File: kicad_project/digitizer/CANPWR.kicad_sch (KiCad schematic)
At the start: 14 parts, among them IC201 MAX3059ASA+T UPSTREAM, IC202 MAX6035AAUR50+T, IC203 MAX3059ASA+T DOWNSTREAM, IC204 MAX6043BAUT33+T, J201 DT15-4P (UPSTREAM), J202 DT06-4S (DOWNSTREAM)

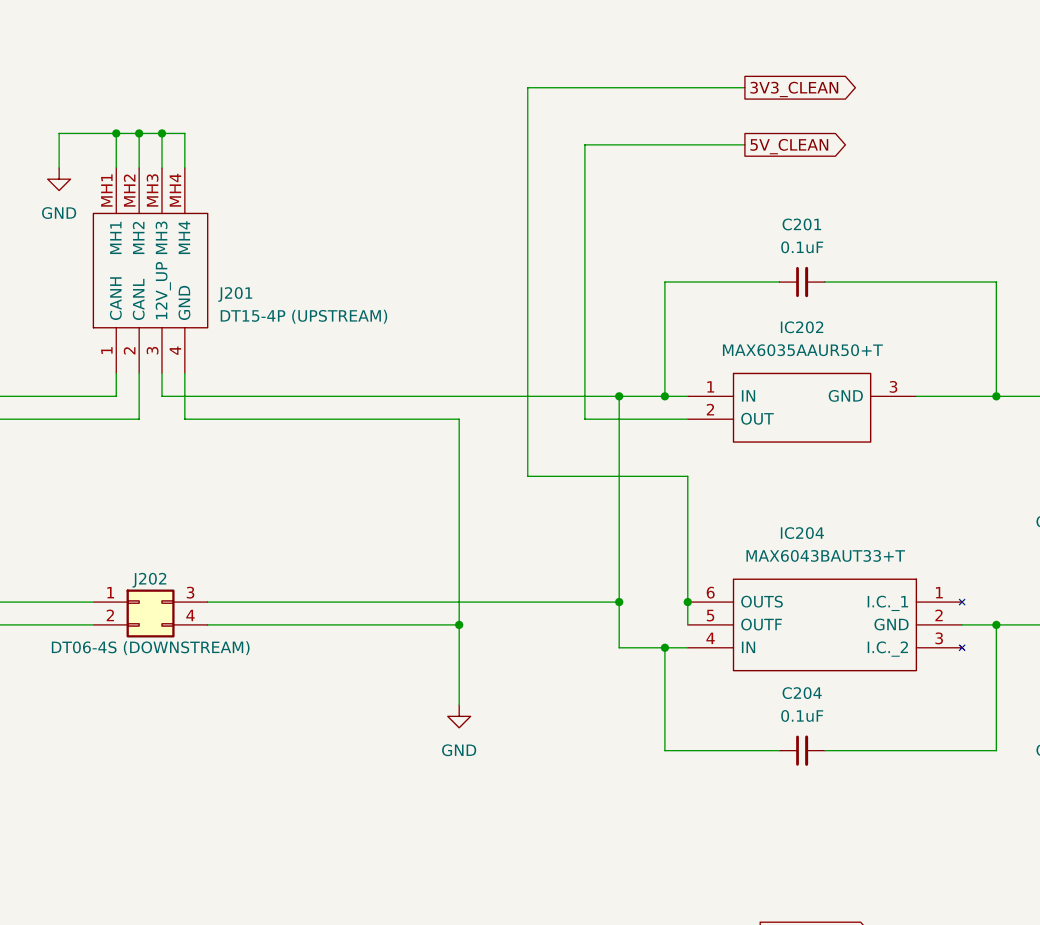
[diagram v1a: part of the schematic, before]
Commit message: added 12V_CLEAN label to schematic; added planes for 12V_CLEAN and 3V3_CLEAN to layout
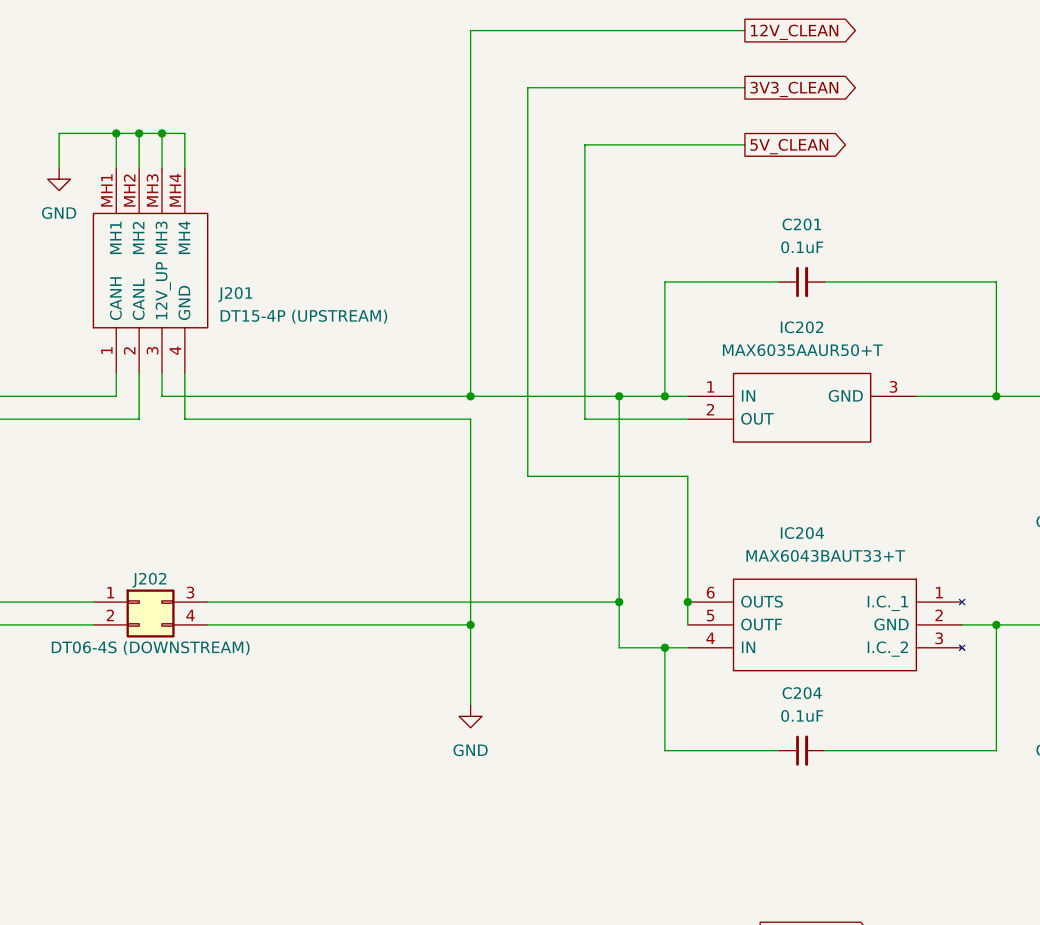
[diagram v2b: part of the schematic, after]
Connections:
- net 12V_CLEAN: now reaches C201.1, C204.1, IC202.1 (IN), IC204.4 (IN), J201.3 (12V_UP), J202.3 (12V_DOWN)
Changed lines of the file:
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@@
   (junction (at 203.2 83.82) (diameter 0) (color 0 0 0 0)
   )
+  (junction (at 186.69 86.36) (diameter 0) (color 0 0 0 0)
+  )
   (junction (at 210.82 83.82) (diameter 0) (color 0 0 0 0)
   )
-  (junction (at 185.42 86.36) (diameter 0) (color 0 0 0 0)
-  )
   (junction (at 208.28 88.9) (diameter 0) (color 0 0 0 0)
   )
@@
   (junction (at 64.77 83.82) (diameter 0) (color 0 0 0 0)
   )
+  (junction (at 186.69 60.96) (diameter 0) (color 0 0 0 0)
+  )
   (junction (at 55.88 86.36) (diameter 0) (color 0 0 0 0)
   )
@@
     (stroke (width 0) (type default) (color 0 0 0 0))
   )
-  (wire (pts (xy 185.42 86.36) (xy 185.42 95.25))
+  (wire (pts (xy 186.69 86.36) (xy 186.69 95.25))
     (stroke (width 0) (type default) (color 0 0 0 0))
   )
@@
     (stroke (width 0) (type default) (color 0 0 0 0))
   )
+  (wire (pts (xy 217.17 20.32) (xy 186.69 20.32))
+    (stroke (width 0) (type default) (color 0 0 0 0))
+  )
   (wire (pts (xy 236.22 129.54) (xy 236.22 133.35))
     (stroke (width 0) (type default) (color 0 0 0 0))
@@
     (stroke (width 0) (type default) (color 0 0 0 0))
   )
-  (wire (pts (xy 154.94 63.5) (xy 185.42 63.5))
+  (wire (pts (xy 154.94 63.5) (xy 186.69 63.5))
     (stroke (width 0) (type default) (color 0 0 0 0))
   )
@@
     (stroke (width 0) (type default) (color 0 0 0 0))
   )
-  (wire (pts (xy 152.4 60.96) (xy 203.2 60.96))
+  (wire (pts (xy 152.4 60.96) (xy 186.69 60.96))
     (stroke (width 0) (type default) (color 0 0 0 0))
   )
@@
     (stroke (width 0) (type default) (color 0 0 0 0))
   )
-  (wire (pts (xy 185.42 63.5) (xy 185.42 86.36))
+  (wire (pts (xy 186.69 63.5) (xy 186.69 86.36))
     (stroke (width 0) (type default) (color 0 0 0 0))
   )
@@
     (stroke (width 0) (type default) (color 0 0 0 0))
   )
+  (wire (pts (xy 186.69 20.32) (xy 186.69 60.96))
+    (stroke (width 0) (type default) (color 0 0 0 0))
+  )
   (wire (pts (xy 251.46 86.36) (xy 251.46 95.25))
     (stroke (width 0) (type default) (color 0 0 0 0))
@@
     (stroke (width 0) (type default) (color 0 0 0 0))
   )
-  (wire (pts (xy 157.48 86.36) (xy 185.42 86.36))
+  (wire (pts (xy 157.48 86.36) (xy 186.69 86.36))
     (stroke (width 0) (type default) (color 0 0 0 0))
   )
@@
   )
   (wire (pts (xy 210.82 63.5) (xy 199.39 63.5))
+    (stroke (width 0) (type default) (color 0 0 0 0))
+  )
+  (wire (pts (xy 186.69 60.96) (xy 203.2 60.96))
     (stroke (width 0) (type default) (color 0 0 0 0))
   )
@@
     (effects (font (size 1.27 1.27)) (justify left))
     (property "Intersheet References" "${INTERSHEET_REFS}" (id 0) (at 228.715 32.9406 0)
+      (effects (font (size 1.27 1.27)) (justify left) hide)
+    )
+  )
+  (global_label "12V_CLEAN" (shape output) (at 217.17 20.32 0) (fields_autoplaced)
+    (effects (font (size 1.27 1.27)) (justify left))
+    (property "Intersheet References" "${INTERSHEET_REFS}" (id 0) (at 229.9245 20.2406 0)
       (effects (font (size 1.27 1.27)) (justify left) hide)
     )
@@
     (pin "6")
   )
-  (symbol (lib_id "power:GND") (at 185.42 95.25 0) (unit 1)
+  (symbol (lib_id "power:GND") (at 186.69 95.25 0) (unit 1)
     (in_bom yes) (on_board yes) (fields_autoplaced)
-    (property "Reference" "#PWR0205" (id 0) (at 185.42 101.6 0)
-      (effects (font (size 1.27 1.27)) hide)
-    )
-    (property "Value" "GND" (id 1) (at 185.42 100.33 0))
-    (property "Footprint" "" (id 2) (at 185.42 95.25 0)
-      (effects (font (size 1.27 1.27)) hide)
-    )
-    (property "Datasheet" "" (id 3) (at 185.42 95.25 0)
-      (effects (font (size 1.27 1.27)) hide)
-    )
+    (property "Reference" "#PWR0205" (id 0) (at 186.69 101.6 0)
+      (effects (font (size 1.27 1.27)) hide)
+    )
+    (property "Value" "GND" (id 1) (at 186.69 100.33 0))
+    (property "Footprint" "" (id 2) (at 186.69 95.25 0)
+      (effects (font (size 1.27 1.27)) hide)
+    )
+    (property "Datasheet" "" (id 3) (at 186.69 95.25 0)
+      (effects (font (size 1.27 1.27)) hide)
+    )

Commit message: updated schematic to use all 0805 parts (both caps and resistors)
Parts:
- C201, C202, C203, C204: footprint Capacitor_SMD:C_2220_5650Metric_Pad1.97x5.40mm_HandSolder -> Capacitor_SMD:C_0805_2012Metric_Pad1.18x1.45mm_HandSolder
- R201, R202, R203: footprint Resistor_SMD:R_2512_6332Metric_Pad1.40x3.35mm_HandSolder -> Resistor_SMD:R_0805_2012Metric_Pad1.20x1.40mm_HandSolder
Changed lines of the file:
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@@
       (effects (font (size 1.27 1.27)) (justify left))
     )
-    (property "Footprint" "Resistor_SMD:R_2512_6332Metric_Pad1.40x3.35mm_HandSolder" (id 2) (at 236.22 127 0)
+    (property "Footprint" "Resistor_SMD:R_0805_2012Metric_Pad1.20x1.40mm_HandSolder" (id 2) (at 236.22 127 0)
       (effects (font (size 1.27 1.27)) hide)
     )
@@
     (property "Reference" "C202" (id 0) (at 62.23 54.61 90))
     (property "Value" "0.1uF" (id 1) (at 62.23 57.15 90))
-    (property "Footprint" "Capacitor_SMD:C_2220_5650Metric_Pad1.97x5.40mm_HandSolder" (id 2) (at 62.23 60.96 0)
+    (property "Footprint" "Capacitor_SMD:C_0805_2012Metric_Pad1.18x1.45mm_HandSolder" (id 2) (at 62.23 60.96 0)
       (effects (font (size 1.27 1.27)) hide)
     )
@@
       (effects (font (size 1.27 1.27)) (justify left))
     )
-    (property "Footprint" "Resistor_SMD:R_2512_6332Metric_Pad1.40x3.35mm_HandSolder" (id 2) (at 97.79 77.47 0)
+    (property "Footprint" "Resistor_SMD:R_0805_2012Metric_Pad1.20x1.40mm_HandSolder" (id 2) (at 97.79 77.47 0)
       (effects (font (size 1.27 1.27)) hide)
     )
@@
       (effects (font (size 1.27 1.27)) (justify left))
     )
-    (property "Footprint" "Resistor_SMD:R_2512_6332Metric_Pad1.40x3.35mm_HandSolder" (id 2) (at 97.79 67.31 0)
+    (property "Footprint" "Resistor_SMD:R_0805_2012Metric_Pad1.20x1.40mm_HandSolder" (id 2) (at 97.79 67.31 0)
       (effects (font (size 1.27 1.27)) hide)
     )
@@
     (property "Reference" "C201" (id 0) (at 223.5263 41.91 90))
     (property "Value" "0.1uF" (id 1) (at 223.5263 44.45 90))
-    (property "Footprint" "Capacitor_SMD:C_2220_5650Metric_Pad1.97x5.40mm_HandSolder" (id 2) (at 223.52 48.26 0)
+    (property "Footprint" "Capacitor_SMD:C_0805_2012Metric_Pad1.18x1.45mm_HandSolder" (id 2) (at 223.52 48.26 0)
       (effects (font (size 1.27 1.27)) hide)
     )
@@
     (property "Reference" "C203" (id 0) (at 62.23 77.47 90))
     (property "Value" "0.1uF" (id 1) (at 62.23 80.01 90))
-    (property "Footprint" "Capacitor_SMD:C_2220_5650Metric_Pad1.97x5.40mm_HandSolder" (id 2) (at 62.23 83.82 0)
+    (property "Footprint" "Capacitor_SMD:C_0805_2012Metric_Pad1.18x1.45mm_HandSolder" (id 2) (at 62.23 83.82 0)
       (effects (font (size 1.27 1.27)) hide)
     )
@@
     (property "Reference" "C204" (id 0) (at 223.5263 93.98 90))
     (property "Value" "0.1uF" (id 1) (at 223.5263 96.52 90))
-    (property "Footprint" "Capacitor_SMD:C_2220_5650Metric_Pad1.97x5.40mm_HandSolder" (id 2) (at 223.52 100.33 0)
-      (effects (font (size 1.27 1.27)) hide)
-    )
+    (property "Footprint" "Capacitor_SMD:C_0805_2012Metric_Pad1.18x1.45mm_HandSolder" (id 2) (at 223.52 100.33 0)
+      (effects (font (size 1.27 1.27)) hide)
+    )

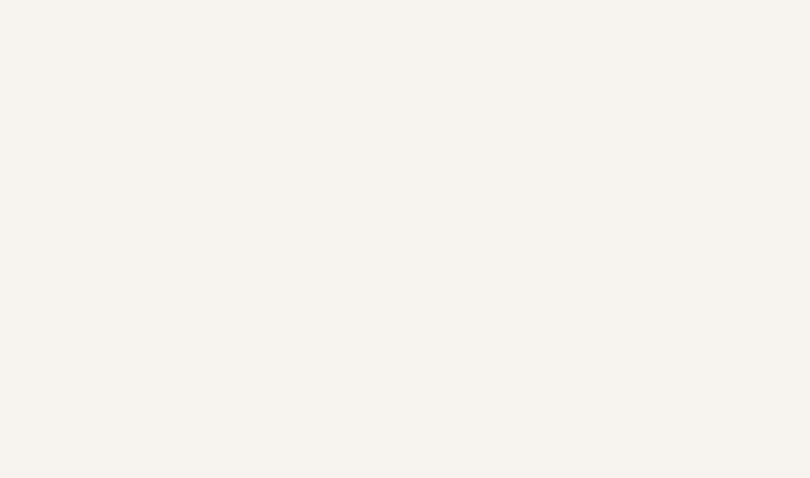
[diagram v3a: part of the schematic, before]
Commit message: properly added mounting holes, drew proper dimension lines
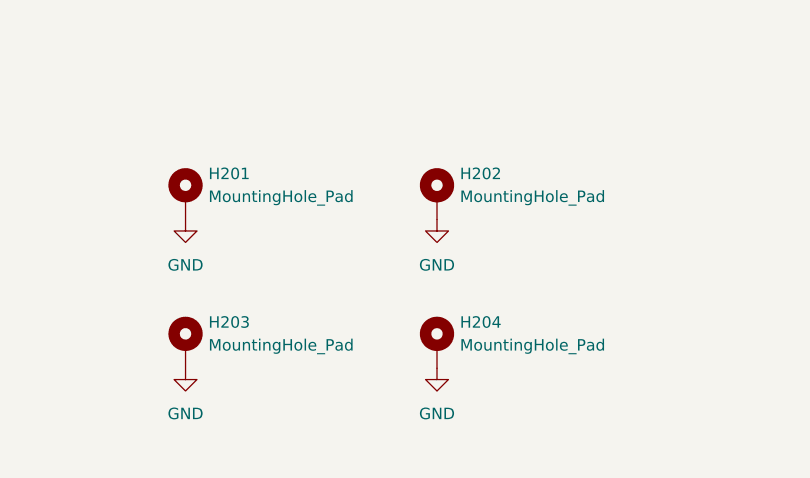
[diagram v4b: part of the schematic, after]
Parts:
- added H201, H202, H203, H204: MountingHole_Pad, MountingHole:MountingHole_3.2mm_M3_Pad, symbol Mechanical:MountingHole_Pad
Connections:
- net GND: now also H201.1, H202.1, H203.1, H204.1
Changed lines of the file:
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@@
     (pin "MH4")
+  )
+  (symbol (lib_id "power:GND") (at 55.88 148.59 0) (unit 1)
+    (in_bom yes) (on_board yes) (fields_autoplaced)
+    (property "Reference" "#PWR0209" (id 0) (at 55.88 154.94 0)
+      (effects (font (size 1.27 1.27)) hide)
+    )
+    (property "Value" "GND" (id 1) (at 55.88 153.67 0))
+    (property "Footprint" "" (id 2) (at 55.88 148.59 0)
+      (effects (font (size 1.27 1.27)) hide)
+    )
+    (property "Datasheet" "" (id 3) (at 55.88 148.59 0)
+      (effects (font (size 1.27 1.27)) hide)
+    )
+    (pin "1")
   )
   (symbol (lib_id "SamacSys_Parts:HLMP-Y802-F0000") (at 236.22 148.59 90) (unit 1)
@@
     (pin "6")
   )
+  (symbol (lib_id "Mechanical:MountingHole_Pad") (at 55.88 129.54 0) (unit 1)
+    (in_bom yes) (on_board yes) (fields_autoplaced)
+    (property "Reference" "H201" (id 0) (at 58.42 126.9999 0)
+      (effects (font (size 1.27 1.27)) (justify left))
+    )
+    (property "Value" "MountingHole_Pad" (id 1) (at 58.42 129.5399 0)
+      (effects (font (size 1.27 1.27)) (justify left))
+    )
+    (property "Footprint" "MountingHole:MountingHole_3.2mm_M3_Pad" (id 2) (at 55.88 129.54 0)
+      (effects (font (size 1.27 1.27)) hide)
+    )
+    (property "Datasheet" "~" (id 3) (at 55.88 129.54 0)
+      (effects (font (size 1.27 1.27)) hide)
+    )
+    (pin "1")
+  )
   (symbol (lib_id "power:GND") (at 186.69 95.25 0) (unit 1)
     (in_bom yes) (on_board yes) (fields_autoplaced)
@@
     )
     (property "Datasheet" "" (id 3) (at 186.69 95.25 0)
+      (effects (font (size 1.27 1.27)) hide)
+    )
+    (pin "1")
+  )
+  (symbol (lib_id "Mechanical:MountingHole_Pad") (at 83.82 146.05 0) (unit 1)
+    (in_bom yes) (on_board yes) (fields_autoplaced)
+    (property "Reference" "H204" (id 0) (at 86.36 143.5099 0)
+      (effects (font (size 1.27 1.27)) (justify left))
+    )
+    (property "Value" "MountingHole_Pad" (id 1) (at 86.36 146.0499 0)
+      (effects (font (size 1.27 1.27)) (justify left))
+    )
+    (property "Footprint" "MountingHole:MountingHole_3.2mm_M3_Pad" (id 2) (at 83.82 146.05 0)
+      (effects (font (size 1.27 1.27)) hide)
+    )
+    (property "Datasheet" "~" (id 3) (at 83.82 146.05 0)
       (effects (font (size 1.27 1.27)) hide)
     )
@@
     (pin "1")
     (pin "2")
+  )
+  (symbol (lib_id "power:GND") (at 83.82 148.59 0) (unit 1)
+    (in_bom yes) (on_board yes) (fields_autoplaced)
+    (property "Reference" "#PWR0210" (id 0) (at 83.82 154.94 0)
+      (effects (font (size 1.27 1.27)) hide)
+    )
+    (property "Value" "GND" (id 1) (at 83.82 153.67 0))
+    (property "Footprint" "" (id 2) (at 83.82 148.59 0)
+      (effects (font (size 1.27 1.27)) hide)
+    )
+    (property "Datasheet" "" (id 3) (at 83.82 148.59 0)
+      (effects (font (size 1.27 1.27)) hide)
+    )
+    (pin "1")
   )
   (symbol (lib_name "MAX3059ASA+T_2") (lib_id "SamacSys_Parts:MAX3059ASA+T") (at 67.31 58.42 0) (unit 1)
@@
     (pin "1")
   )
+  (symbol (lib_id "power:GND") (at 55.88 132.08 0) (unit 1)
+    (in_bom yes) (on_board yes) (fields_autoplaced)
+    (property "Reference" "#PWR0207" (id 0) (at 55.88 138.43 0)
+      (effects (font (size 1.27 1.27)) hide)
+    )
+    (property "Value" "GND" (id 1) (at 55.88 137.16 0))
+    (property "Footprint" "" (id 2) (at 55.88 132.08 0)
+      (effects (font (size 1.27 1.27)) hide)
+    )
+    (property "Datasheet" "" (id 3) (at 55.88 132.08 0)
+      (effects (font (size 1.27 1.27)) hide)
+    )
+    (pin "1")
+  )
   (symbol (lib_id "power:GND") (at 236.22 152.4 0) (unit 1)
     (in_bom yes) (on_board yes) (fields_autoplaced)
-    (property "Reference" "#PWR0207" (id 0) (at 236.22 158.75 0)
+    (property "Reference" "#PWR0211" (id 0) (at 236.22 158.75 0)
       (effects (font (size 1.27 1.27)) hide)
     )
@@
     (pin "4")
   )
+  (symbol (lib_id "Mechanical:MountingHole_Pad") (at 55.88 146.05 0) (unit 1)
+    (in_bom yes) (on_board yes) (fields_autoplaced)
+    (property "Reference" "H203" (id 0) (at 58.42 143.5099 0)
+      (effects (font (size 1.27 1.27)) (justify left))
+    )
+    (property "Value" "MountingHole_Pad" (id 1) (at 58.42 146.0499 0)
+      (effects (font (size 1.27 1.27)) (justify left))
+    )
+    (property "Footprint" "MountingHole:MountingHole_3.2mm_M3_Pad" (id 2) (at 55.88 146.05 0)
+      (effects (font (size 1.27 1.27)) hide)
+    )
+    (property "Datasheet" "~" (id 3) (at 55.88 146.05 0)
+      (effects (font (size 1.27 1.27)) hide)
+    )
+    (pin "1")
+  )
   (symbol (lib_id "Device:C_Small") (at 62.23 83.82 270) (unit 1)
     (in_bom yes) (on_board yes)
@@
     (pin "2")
   )
+  (symbol (lib_id "power:GND") (at 83.82 132.08 0) (unit 1)
+    (in_bom yes) (on_board yes) (fields_autoplaced)
+    (property "Reference" "#PWR0208" (id 0) (at 83.82 138.43 0)
+      (effects (font (size 1.27 1.27)) hide)
+    )
+    (property "Value" "GND" (id 1) (at 83.82 137.16 0))
+    (property "Footprint" "" (id 2) (at 83.82 132.08 0)
+      (effects (font (size 1.27 1.27)) hide)
+    )
+    (property "Datasheet" "" (id 3) (at 83.82 132.08 0)
+      (effects (font (size 1.27 1.27)) hide)
+    )
+    (pin "1")
+  )
+  (symbol (lib_id "Mechanical:MountingHole_Pad") (at 83.82 129.54 0) (unit 1)
+    (in_bom yes) (on_board yes) (fields_autoplaced)
+    (property "Reference" "H202" (id 0) (at 86.36 126.9999 0)
+      (effects (font (size 1.27 1.27)) (justify left))
+    )
+    (property "Value" "MountingHole_Pad" (id 1) (at 86.36 129.5399 0)
+      (effects (font (size 1.27 1.27)) (justify left))
+    )
+    (property "Footprint" "MountingHole:MountingHole_3.2mm_M3_Pad" (id 2) (at 83.82 129.54 0)
+      (effects (font (size 1.27 1.27)) hide)
+    )
+    (property "Datasheet" "~" (id 3) (at 83.82 129.54 0)
+      (effects (font (size 1.27 1.27)) hide)
+    )
+    (pin "1")
+  )
 )
